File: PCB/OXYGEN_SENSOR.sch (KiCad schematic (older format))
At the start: 7 parts, among them J15 OXYGEN_CONN, U22 MCP6001-OT

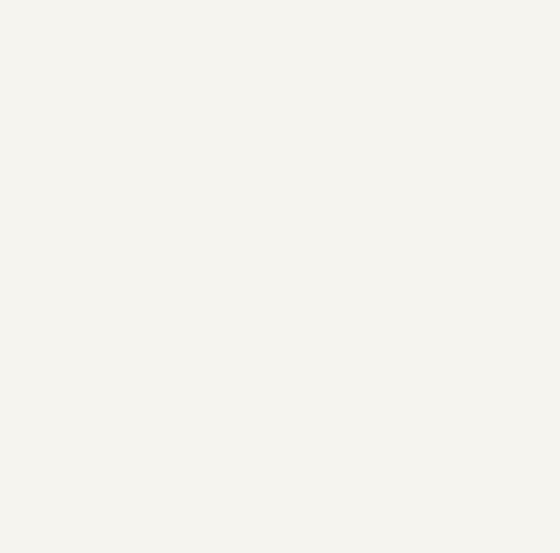
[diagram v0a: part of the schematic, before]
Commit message: Added virtual oxygen sensor and connector footprint
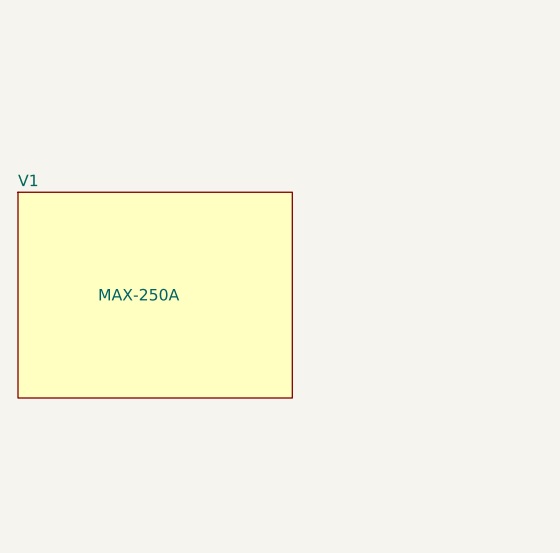
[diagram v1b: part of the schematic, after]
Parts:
- added V1: MAX-250A, symbol custom:VIRTUAL_PART
- J15: footprint (none) -> custom:A-2014-3-4-N-T-R
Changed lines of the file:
@@
 F 0 "J15" H 4757 4167 50  0000 C CNN
 F 1 "OXYGEN_CONN" H 4757 4076 50  0000 C CNN
-F 2 "" V 4700 3750 50  0001 C CNN
+F 2 "custom:A-2014-3-4-N-T-R" V 4700 3750 50  0001 C CNN
 F 3 "http://www.assmann-wsw.com/fileadmin/datasheets/ASS_7331_CO.pdf" V 4700 3750 50  0001 C CNN
 F 4 "A-2014-3-4-N-T-R" H 4700 3700 50  0001 C CNN "MPN"
@@
 Wire Wire Line
 	5500 3700 6350 3700
+$Comp
+L custom:VIRTUAL_PART V1
+U 1 1 5E9C195B
+P 2500 3650
+F 0 "V1" H 1900 4150 50  0000 L CNN
+F 1 "MAX-250A" H 2250 3650 50  0000 L CNN
+F 2 "" H 2500 3650 50  0001 C CNN
+F 3 "https://cdn.maxtec.com/product-docs/max-250a-250m-250l-specifications.pdf" H 2500 3650 50  0001 C CNN
+	1    2500 3650
+	1    0    0    -1
+$EndComp
 $EndSCHEMATC

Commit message: Added some footprints
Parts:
- C56, C57: footprint (none) -> Capacitor_SMD:C_0603_1608Metric; Dielectric (none) -> X7R; Voltage Rating (none) -> 6.3V
- R47, R48, R49: footprint (none) -> Resistor_SMD:R_0603_1608Metric
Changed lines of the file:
@@
 F 0 "R48" V 6154 3900 50  0000 C CNN
 F 1 "1k" V 6245 3900 50  0000 C CNN
-F 2 "" H 6050 3900 50  0001 C CNN
+F 2 "Resistor_SMD:R_0603_1608Metric" H 6050 3900 50  0001 C CNN
 F 3 "~" H 6050 3900 50  0001 C CNN
 	1    6050 3900
@@
 F 0 "R49" V 6704 4450 50  0000 C CNN
 F 1 "100k" V 6795 4450 50  0000 C CNN
-F 2 "" H 6600 4450 50  0001 C CNN
+F 2 "Resistor_SMD:R_0603_1608Metric" H 6600 4450 50  0001 C CNN
 F 3 "~" H 6600 4450 50  0001 C CNN
 	1    6600 4450
@@
 F 0 "R47" H 5441 3304 50  0000 R CNN
 F 1 "10k" H 5441 3395 50  0000 R CNN
-F 2 "" H 5500 3350 50  0001 C CNN
+F 2 "Resistor_SMD:R_0603_1608Metric" H 5500 3350 50  0001 C CNN
 F 3 "~" H 5500 3350 50  0001 C CNN
 	1    5500 3350
@@
 F 0 "C56" H 6642 2846 50  0000 L CNN
 F 1 "100nF" H 6642 2755 50  0000 L CNN
-F 2 "" H 6550 2800 50  0001 C CNN
+F 2 "Capacitor_SMD:C_0603_1608Metric" H 6550 2800 50  0001 C CNN
 F 3 "~" H 6550 2800 50  0001 C CNN
+F 4 "X7R" H 6550 2800 50  0001 C CNN "Dielectric"
+F 5 "6.3V" H 6550 2800 50  0001 C CNN "Voltage Rating"
 	1    6550 2800
 	1    0    0    -1
@@
 F 0 "C57" H 5409 4046 50  0000 R CNN
 F 1 "10nF" H 5409 3955 50  0000 R CNN
-F 2 "" H 5500 4000 50  0001 C CNN
+F 2 "Capacitor_SMD:C_0603_1608Metric" H 5500 4000 50  0001 C CNN
 F 3 "~" H 5500 4000 50  0001 C CNN
+F 4 "X7R" H 5500 4000 50  0001 C CNN "Dielectric"
+F 5 "6.3V" H 5500 4000 50  0001 C CNN "Voltage Rating"
 	1    5500 4000
 	1    0    0    -1
